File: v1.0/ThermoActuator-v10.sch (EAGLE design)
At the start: 75 parts, among them IC1 ULN2003AD, IC2 LM358D, IC3 LM358D, IC4 LM358D, IC5 LM358D

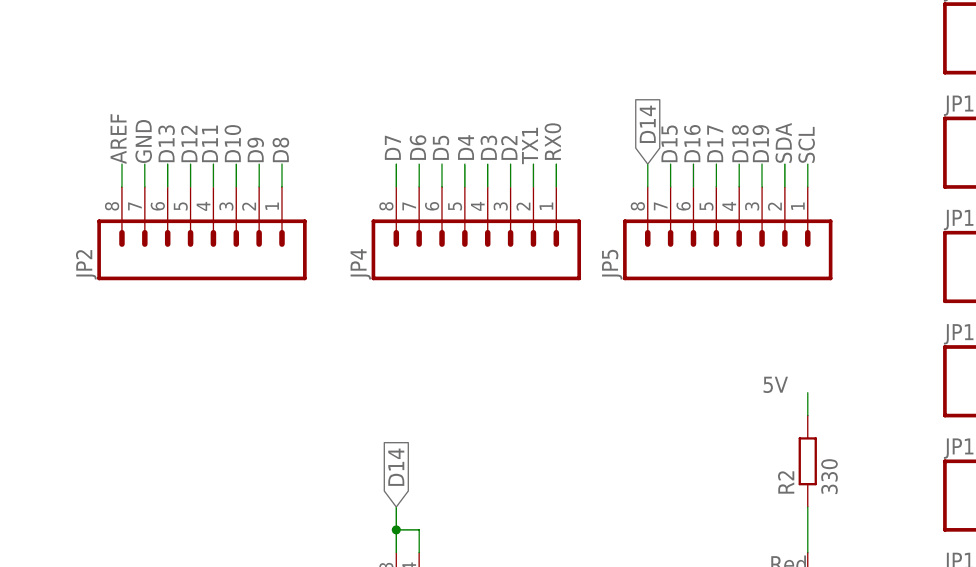
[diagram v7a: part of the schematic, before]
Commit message: relay power manual route
this commit fixes one flipped connector, lines up
the connectors on 0,1mm grid (as per Mega board)

the board is almost ready for ordering
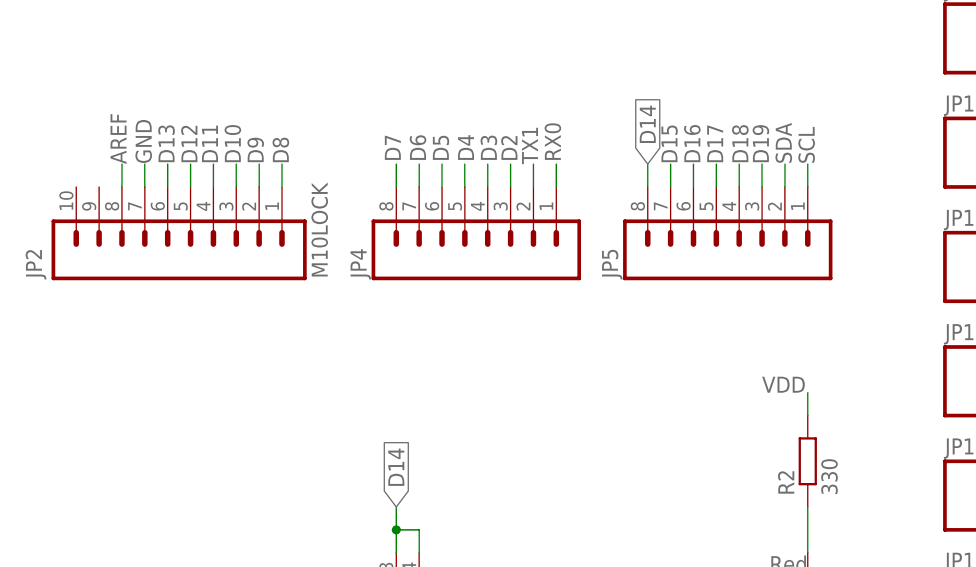
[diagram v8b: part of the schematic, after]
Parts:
- JP2: value (none) -> M10LOCK; device SparkFun:M08LOCK -> SparkFun-Connectors:M10LOCK
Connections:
- net 5V: no longer R2.2
- net VDD: now also R2.2
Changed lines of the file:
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@@
 <parts>
 <part name="FRAME1" library="SparkFun" deviceset="FRAME-LETTER" device=""/>
-<part name="JP2" library="SparkFun" deviceset="M08" device="LOCK"/>
+<part name="JP2" library="SparkFun-Connectors" deviceset="M10" device="LOCK"/>
 <part name="JP4" library="SparkFun" deviceset="M08" device="LOCK"/>
 <part name="JP5" library="SparkFun" deviceset="M08" device="LOCK"/>
@@
 <instance part="FRAME1" gate="G$1" x="0" y="0"/>
 <instance part="FRAME1" gate="G$2" x="147.32" y="0"/>
-<instance part="JP2" gate="G$1" x="30.48" y="127" rot="R90"/>
+<instance part="JP2" gate="G$1" x="20.32" y="121.92" rot="R90"/>
 <instance part="JP4" gate="G$1" x="60.96" y="127" rot="R90"/>
 <instance part="JP5" gate="G$1" x="88.9" y="127" rot="R90"/>
@@
 <pinref part="JP1" gate="G$1" pin="3"/>
 </segment>
-<segment>
-<wire x1="96.52" y1="106.68" x2="96.52" y2="109.22" width="0.1524" layer="91"/>
-<label x="91.44" y="109.22" size="1.778" layer="95"/>
-<pinref part="R2" gate="G$1" pin="2"/>
-</segment>
 </net>
 <net name="GND" class="0">
@@
 <wire x1="236.22" y1="180.34" x2="236.22" y2="177.8" width="0.1524" layer="91"/>
 </segment>
-</net>
+<segment>
+<wire x1="96.52" y1="106.68" x2="96.52" y2="109.22" width="0.1524" layer="91"/>
+<label x="91.44" y="109.22" size="1.778" layer="95"/>
+<pinref part="R2" gate="G$1" pin="2"/>
+</segment>
+</net>
